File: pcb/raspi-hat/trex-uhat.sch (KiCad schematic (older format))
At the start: 17 parts, among them J1 Conn_01x08_Female, J10 RAIL2, J2 RPi_GPIO, J3 Conn_01x03_Female, J4 DFPLAYER_MINI, J5 RAIL1, J6 Conn_01x04_Female, J7 AudioJack3, J8 Jack-DC, J9 Conn_01x05_Female

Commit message: fix(pcb): motor connections, replace audio + power jacks
- Change power jack from PJ-063AH to the smaller PJ-102AH
- Change audio jack from SJ1-3533NG to PJ320E
- Fix motor connections: connect Pi to ~SLP instead of EN
- Improve DFPlayer Mini Footprint
- Add silk-screen texts
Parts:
- J7: footprint Connector_Audio:Jack_3.5mm_CUI_SJ1-3533NG_Horizontal -> Connector_Audio:Jack_3.5mm_PJ320E_Horizontal; symbol Connector:AudioJack3 -> Connector:AudioJack4
- J8: footprint Connector_BarrelJack:BarrelJack_CUI_PJ-063AH_Horizontal -> Connector_BarrelJack:BarrelJack_CUI_PJ-102AH_Horizontal
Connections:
- net labels added: STP1_~SLP, STP2_~SLP
- net labels removed: STP1_EN, STP2_EN
- wire segments 114 -> 118
- no-connect marks 36 -> 37
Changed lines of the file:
@@
 	7300 3300 6800 3300
 Text Label 6800 3300 0    50   ~ 0
-STP1_EN
+STP1_~SLP
 Wire Wire Line
 	7300 3400 6800 3400
@@
 STP1_STEP
 Wire Wire Line
-	3250 6050 2850 6050
-Wire Wire Line
-	3250 5850 2850 5850
-Text Label 2850 5850 0    50   ~ 0
-STP1_EN
-Text Label 2850 5950 0    50   ~ 0
+	3250 6050 2800 6050
+Text Label 2800 5650 0    50   ~ 0
+STP1_~SLP
+Text Label 2800 5950 0    50   ~ 0
 STP1_STEP
 Wire Wire Line
-	2850 5950 3250 5950
-Text Label 2850 6050 0    50   ~ 0
+	2800 5950 3250 5950
+Text Label 2800 6050 0    50   ~ 0
 STP1_DIR
-Wire Wire Line
-	4850 5900 5300 5900
-Text Label 4850 5900 0    50   ~ 0
-STP2_EN
+Text Label 4850 5700 0    50   ~ 0
+STP2_~SLP
 Wire Wire Line
 	5300 6000 4850 6000
@@
 	7300 4200 6800 4200
 Text Label 6800 4200 0    50   ~ 0
-STP2_EN
+STP2_~SLP
 Wire Wire Line
 	9200 4200 9650 4200
@@
 NoConn ~ 1650 2600
 $Comp
-L Connector:AudioJack3 J7
+L Connector:AudioJack4 J7
 U 1 1 5D77E4B7
 P 1100 3550
 F 0 "J7" V 1128 3320 50  0000 R CNN
 F 1 "AudioJack3" V 1037 3320 50  0000 R CNN
-F 2 "Connector_Audio:Jack_3.5mm_CUI_SJ1-3533NG_Horizontal" H 1100 3550 50  0001 C CNN
+F 2 "Connector_Audio:Jack_3.5mm_PJ320E_Horizontal" H 1100 3550 50  0001 C CNN
 F 3 "~" H 1100 3550 50  0001 C CNN
 	1    1100 3550
 	0    -1   -1   0
 $EndComp
-Wire Wire Line
-	1650 3100 1000 3100
-Wire Wire Line
-	1000 3100 1000 3350
-Wire Wire Line
-	1100 3350 1200 3350
-Wire Wire Line
-	1100 3350 1100 2900
-Wire Wire Line
-	1100 2900 1650 2900
-Connection ~ 1100 3350
 $Comp
 L Connector:Barrel_Jack_Switch J8
@@
 F 0 "J8" H 8970 1500 50  0000 R CNN
 F 1 "Jack-DC" H 8970 1591 50  0000 R CNN
-F 2 "Connector_BarrelJack:BarrelJack_CUI_PJ-063AH_Horizontal" H 9250 1510 50  0001 C CNN
+F 2 "Connector_BarrelJack:BarrelJack_CUI_PJ-102AH_Horizontal" H 9250 1510 50  0001 C CNN
 F 3 "~" H 9250 1510 50  0001 C CNN
 	1    9200 1550
@@
 NoConn ~ 3250 6450
 NoConn ~ 3250 6550
-NoConn ~ 3250 5650
+NoConn ~ 3250 5850
 NoConn ~ 3250 5550
 NoConn ~ 5300 5600
-NoConn ~ 5300 5700
+NoConn ~ 5300 5900
 $Comp
 L Connector:Conn_01x04_Female J10
@@
 	9450 4900 9300 4900
 $Comp
-L power:+3.3V #PWR?
+L power:+3.3V #PWR0106
 U 1 1 5D910A9E
 P 10150 5100
-F 0 "#PWR?" H 10150 4950 50  0001 C CNN
+F 0 "#PWR0106" H 10150 4950 50  0001 C CNN
 F 1 "+3.3V" H 10165 5273 50  0000 C CNN
 F 2 "" H 10150 5100 50  0001 C CNN
@@
 Wire Wire Line
 	10150 4900 10150 5100
+Wire Wire Line
+	1000 2900 1000 3250
+Wire Wire Line
+	1000 2900 1650 2900
+Wire Wire Line
+	1650 3100 1300 3100
+Wire Wire Line
+	1200 3100 1200 3350
+Wire Wire Line
+	1300 3350 1300 3100
+Connection ~ 1300 3100
+Wire Wire Line
+	1300 3100 1200 3100
+Wire Wire Line
+	1000 3250 1100 3250
+Wire Wire Line
+	1100 3250 1100 3350
+Connection ~ 1000 3250
+Wire Wire Line
+	1000 3250 1000 3350
+Wire Wire Line
+	3250 5650 2800 5650
+Wire Wire Line
+	5300 5700 4850 5700
+NoConn ~ 9750 5200
 $EndSCHEMATC

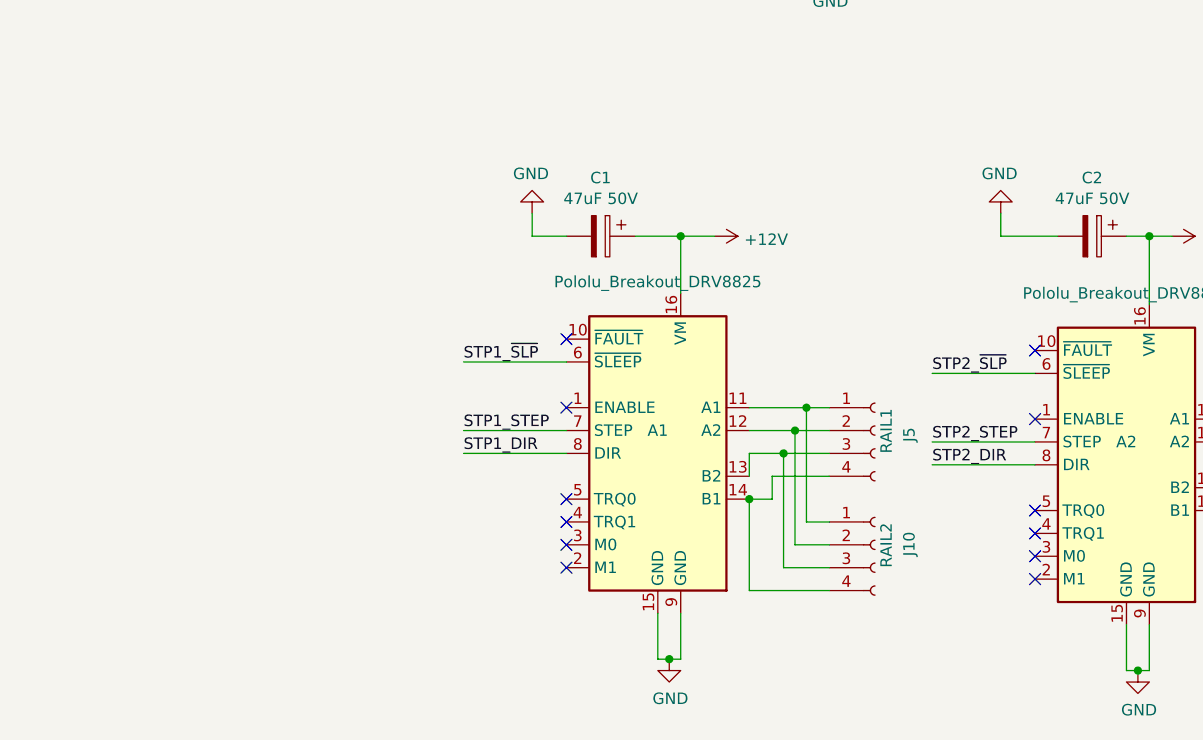
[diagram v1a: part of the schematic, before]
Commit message: feat(pcb): DRV8825 support
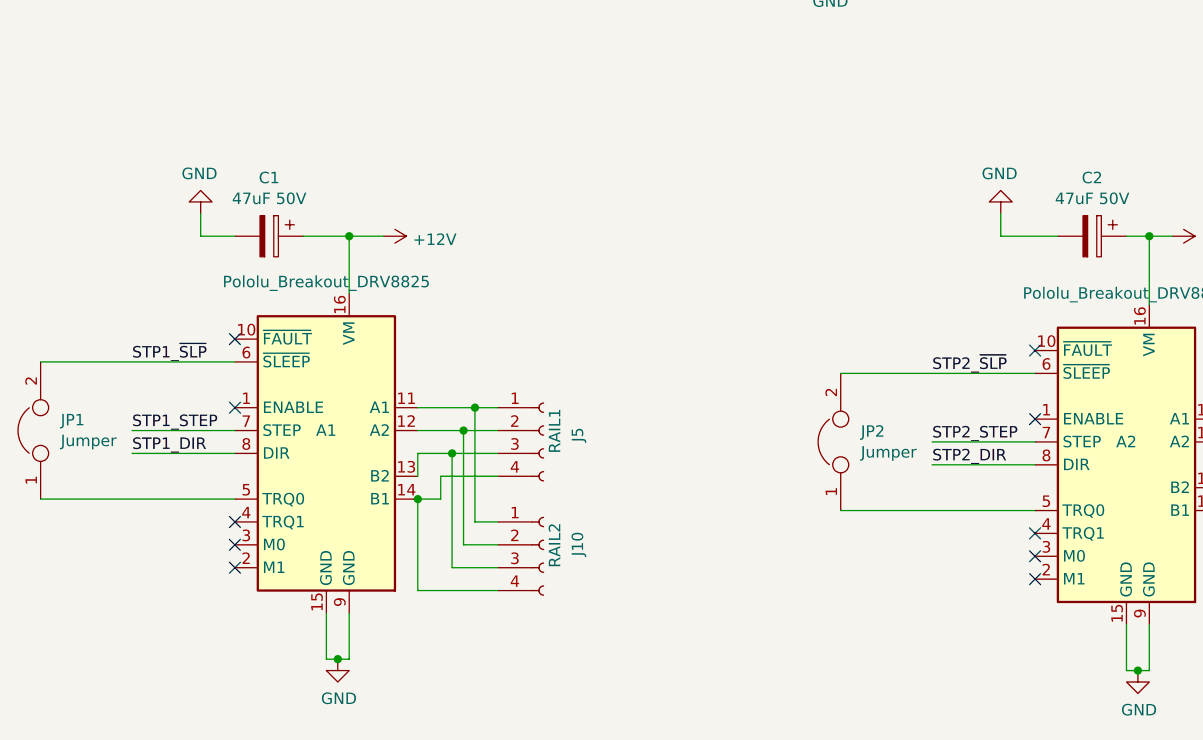
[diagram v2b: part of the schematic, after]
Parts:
- added JP1, JP2: Jumper, Jumper:SolderJumper-2_P1.3mm_Bridged_RoundedPad1.0x1.5mm, symbol Device:Jumper
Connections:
- wire segments 118 -> 120
- no-connect marks 37 -> 35
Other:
- moved on the sheet: A1, C1, J10, J5
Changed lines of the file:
@@
 L uhat:Pololu_Breakout_DRV8880 A1
 U 1 1 5D6AAAE1
-P 3650 5950
-F 0 "A1" H 3650 5950 50  0000 C CNN
-F 1 "Pololu_Breakout_DRV8825" H 3650 6600 50  0000 C CNN
-F 2 "Module:Pololu_Breakout-16_15.2x20.3mm" H 3850 5150 50  0001 L CNN
-F 3 "https://www.pololu.com/product/2982" H 3750 5650 50  0001 C CNN
-	1    3650 5950
+P 2200 5950
+F 0 "A1" H 2200 5950 50  0000 C CNN
+F 1 "Pololu_Breakout_DRV8825" H 2200 6600 50  0000 C CNN
+F 2 "Module:Pololu_Breakout-16_15.2x20.3mm" H 2400 5150 50  0001 L CNN
+F 3 "https://www.pololu.com/product/2982" H 2300 5650 50  0001 C CNN
+	1    2200 5950
 	1    0    0    -1
 $EndComp
@@
 L power:GND #PWR06
 U 1 1 5D6B2DDB
-P 3700 6950
-F 0 "#PWR06" H 3700 6700 50  0001 C CNN
-F 1 "GND" H 3705 6777 50  0000 C CNN
-F 2 "" H 3700 6950 50  0001 C CNN
-F 3 "" H 3700 6950 50  0001 C CNN
-	1    3700 6950
-	1    0    0    -1
-$EndComp
-Wire Wire Line
-	3750 6750 3750 6950
-Wire Wire Line
-	3750 6950 3700 6950
-Wire Wire Line
-	3700 6950 3650 6950
-Wire Wire Line
-	3650 6950 3650 6750
-Connection ~ 3700 6950
+P 2250 6950
+F 0 "#PWR06" H 2250 6700 50  0001 C CNN
+F 1 "GND" H 2255 6777 50  0000 C CNN
+F 2 "" H 2250 6950 50  0001 C CNN
+F 3 "" H 2250 6950 50  0001 C CNN
+	1    2250 6950
+	1    0    0    -1
+$EndComp
+Wire Wire Line
+	2300 6750 2300 6950
+Wire Wire Line
+	2300 6950 2250 6950
+Wire Wire Line
+	2250 6950 2200 6950
+Wire Wire Line
+	2200 6950 2200 6750
+Connection ~ 2250 6950
 $Comp
 L power:+12V #PWR011
@@
 L Device:CP C1
 U 1 1 5D6CC610
-P 3400 5100
-F 0 "C1" V 3145 5100 50  0000 C CNN
-F 1 "47uF 50V" V 3236 5100 50  0000 C CNN
-F 2 "Capacitor_THT:CP_Radial_D6.3mm_P2.50mm" H 3438 4950 50  0001 C CNN
-F 3 "~" H 3400 5100 50  0001 C CNN
-	1    3400 5100
+P 1950 5100
+F 0 "C1" V 1695 5100 50  0000 C CNN
+F 1 "47uF 50V" V 1786 5100 50  0000 C CNN
+F 2 "Capacitor_THT:CP_Radial_D6.3mm_P2.50mm" H 1988 4950 50  0001 C CNN
+F 3 "~" H 1950 5100 50  0001 C CNN
+	1    1950 5100
 	0    1    1    0
 $EndComp
@@
 L power:+12V #PWR08
 U 1 1 5D6CCA76
-P 3900 5100
-F 0 "#PWR08" H 3900 4950 50  0001 C CNN
-F 1 "+12V" V 3915 5228 50  0000 L CNN
-F 2 "" H 3900 5100 50  0001 C CNN
-F 3 "" H 3900 5100 50  0001 C CNN
-	1    3900 5100
-	0    1    1    0
-$EndComp
-Wire Wire Line
-	3900 5100 3750 5100
-Wire Wire Line
-	3750 5350 3750 5100
-Connection ~ 3750 5100
-Wire Wire Line
-	3750 5100 3550 5100
+P 2450 5100
+F 0 "#PWR08" H 2450 4950 50  0001 C CNN
+F 1 "+12V" V 2465 5228 50  0000 L CNN
+F 2 "" H 2450 5100 50  0001 C CNN
+F 3 "" H 2450 5100 50  0001 C CNN
+	1    2450 5100
+	0    1    1    0
+$EndComp
+Wire Wire Line
+	2450 5100 2300 5100
+Wire Wire Line
+	2300 5350 2300 5100
+Connection ~ 2300 5100
+Wire Wire Line
+	2300 5100 2100 5100
 Wire Wire Line
 	5700 5100 5800 5100
@@
 L power:GND #PWR05
 U 1 1 5D6D45D1
-P 3100 5000
-F 0 "#PWR05" H 3100 4750 50  0001 C CNN
-F 1 "GND" H 3105 4827 50  0000 C CNN
-F 2 "" H 3100 5000 50  0001 C CNN
-F 3 "" H 3100 5000 50  0001 C CNN
-	1    3100 5000
+P 1650 5000
+F 0 "#PWR05" H 1650 4750 50  0001 C CNN
+F 1 "GND" H 1655 4827 50  0000 C CNN
+F 2 "" H 1650 5000 50  0001 C CNN
+F 3 "" H 1650 5000 50  0001 C CNN
+	1    1650 5000
 	-1   0    0    1
 $EndComp
 Wire Wire Line
-	3250 5100 3100 5100
-Wire Wire Line
-	3100 5100 3100 5000
+	1800 5100 1650 5100
+Wire Wire Line
+	1650 5100 1650 5000
 $Comp
 L power:GND #PWR09
@@
 	6350 6300 6100 6300
 Wire Wire Line
-	4400 5950 4250 5950
-Wire Wire Line
-	4050 6050 4050 6150
-Wire Wire Line
-	4150 6250 4050 6250
+	2950 5950 2800 5950
+Wire Wire Line
+	2600 6050 2600 6150
+Wire Wire Line
+	2700 6250 2600 6250
 $Comp
 L power:+5V #PWR03
@@
 STP1_STEP
 Wire Wire Line
-	3250 6050 2800 6050
-Text Label 2800 5650 0    50   ~ 0
+	1800 6050 1350 6050
+Text Label 1350 5650 0    50   ~ 0
 STP1_~SLP
-Text Label 2800 5950 0    50   ~ 0
+Text Label 1350 5950 0    50   ~ 0
 STP1_STEP
 Wire Wire Line
-	2800 5950 3250 5950
-Text Label 2800 6050 0    50   ~ 0
+	1350 5950 1800 5950
+Text Label 1350 6050 0    50   ~ 0
 STP1_DIR
 Text Label 4850 5700 0    50   ~ 0
@@
 	8900 1550 8900 1450
 Connection ~ 8900 1450
-NoConn ~ 5300 6300
 NoConn ~ 5300 6400
 NoConn ~ 5300 6500
 NoConn ~ 5300 6600
-NoConn ~ 3250 6250
-NoConn ~ 3250 6350
-NoConn ~ 3250 6450
-NoConn ~ 3250 6550
-NoConn ~ 3250 5850
-NoConn ~ 3250 5550
+NoConn ~ 1800 6350
+NoConn ~ 1800 6450
+NoConn ~ 1800 6550
+NoConn ~ 1800 5850
+NoConn ~ 1800 5550
 NoConn ~ 5300 5600
 NoConn ~ 5300 5900
@@
 L Connector:Conn_01x04_Female J10
 U 1 1 5D85E9E8
-P 4600 6450
-F 0 "J10" V 4750 6400 50  0000 L CNN
-F 1 "RAIL2" V 4650 6350 50  0000 L CNN
-F 2 "Connector_PinSocket_2.54mm:PinSocket_1x04_P2.54mm_Vertical" H 4600 6450 50  0001 C CNN
-F 3 "~" H 4600 6450 50  0001 C CNN
-	1    4600 6450
-	1    0    0    -1
-$EndComp
-Wire Wire Line
-	4050 5850 4300 5850
+P 3150 6450
+F 0 "J10" V 3300 6400 50  0000 L CNN
+F 1 "RAIL2" V 3200 6350 50  0000 L CNN
+F 2 "Connector_PinSocket_2.54mm:PinSocket_1x04_P2.54mm_Vertical" H 3150 6450 50  0001 C CNN
+F 3 "~" H 3150 6450 50  0001 C CNN
+	1    3150 6450
+	1    0    0    -1
+$EndComp
+Wire Wire Line
+	2600 5850 2850 5850
 $Comp
 L Connector:Conn_01x04_Female J5
 U 1 1 5D6D6AFB
-P 4600 5950
-F 0 "J5" V 4750 5900 50  0000 L CNN
-F 1 "RAIL1" V 4650 5850 50  0000 L CNN
-F 2 "Connector_PinSocket_2.54mm:PinSocket_1x04_P2.54mm_Vertical" H 4600 5950 50  0001 C CNN
-F 3 "~" H 4600 5950 50  0001 C CNN
-	1    4600 5950
-	1    0    0    -1
-$EndComp
-Wire Wire Line
-	4400 6150 4150 6150
-Wire Wire Line
-	4050 6250 4050 6650
-Wire Wire Line
-	4050 6650 4400 6650
-Connection ~ 4050 6250
-Wire Wire Line
-	4400 6050 4200 6050
-Wire Wire Line
-	4150 6150 4150 6250
-Wire Wire Line
-	4400 6550 4200 6550
-Wire Wire Line
-	4200 6550 4200 6050
-Connection ~ 4200 6050
-Wire Wire Line
-	4200 6050 4050 6050
-Wire Wire Line
-	4400 6450 4250 6450
-Wire Wire Line
-	4250 6450 4250 5950
-Connection ~ 4250 5950
-Wire Wire Line
-	4250 5950 4050 5950
-Wire Wire Line
-	4300 5850 4300 6350
-Wire Wire Line
-	4300 6350 4400 6350
-Connection ~ 4300 5850
-Wire Wire Line
-	4300 5850 4400 5850
+P 3150 5950
+F 0 "J5" V 3300 5900 50  0000 L CNN
+F 1 "RAIL1" V 3200 5850 50  0000 L CNN
+F 2 "Connector_PinSocket_2.54mm:PinSocket_1x04_P2.54mm_Vertical" H 3150 5950 50  0001 C CNN
+F 3 "~" H 3150 5950 50  0001 C CNN
+	1    3150 5950
+	1    0    0    -1
+$EndComp
+Wire Wire Line
+	2950 6150 2700 6150
+Wire Wire Line
+	2600 6250 2600 6650
+Wire Wire Line
+	2600 6650 2950 6650
+Connection ~ 2600 6250
+Wire Wire Line
+	2950 6050 2750 6050
+Wire Wire Line
+	2700 6150 2700 6250
+Wire Wire Line
+	2950 6550 2750 6550
+Wire Wire Line
+	2750 6550 2750 6050
+Connection ~ 2750 6050
+Wire Wire Line
+	2750 6050 2600 6050
+Wire Wire Line
+	2950 6450 2800 6450
+Wire Wire Line
+	2800 6450 2800 5950
+Connection ~ 2800 5950
+Wire Wire Line
+	2800 5950 2600 5950
+Wire Wire Line
+	2850 5850 2850 6350
+Wire Wire Line
+	2850 6350 2950 6350
+Connection ~ 2850 5850
+Wire Wire Line
+	2850 5850 2950 5850
 Wire Wire Line
 	6950 1650 6950 1800
@@
 Wire Wire Line
 	1000 3250 1000 3350
-Wire Wire Line
-	3250 5650 2800 5650
-Wire Wire Line
-	5300 5700 4850 5700
 NoConn ~ 9750 5200
+$Comp
+L Device:Jumper JP1
+U 1 1 5D895BFF
+P 950 5950
+F 0 "JP1" V 996 5862 50  0000 R CNN
+F 1 "Jumper" V 905 5862 50  0000 R CNN
+F 2 "Jumper:SolderJumper-2_P1.3mm_Bridged_RoundedPad1.0x1.5mm" H 950 5950 50  0001 C CNN
+F 3 "~" H 950 5950 50  0001 C CNN
+	1    950  5950
+	0    -1   -1   0
+$EndComp
+Wire Wire Line
+	950  5650 1800 5650
+Wire Wire Line
+	950  6250 1800 6250
+$Comp
+L Device:Jumper JP2
+U 1 1 5D8AD796
+P 4450 6000
+F 0 "JP2" V 4496 5912 50  0000 R CNN
+F 1 "Jumper" V 4405 5912 50  0000 R CNN
+F 2 "Jumper:SolderJumper-2_P1.3mm_Bridged_RoundedPad1.0x1.5mm" H 4450 6000 50  0001 C CNN
+F 3 "~" H 4450 6000 50  0001 C CNN
+	1    4450 6000
+	0    -1   -1   0
+$EndComp
+Wire Wire Line
+	4450 5700 5300 5700
+Wire Wire Line
+	4450 6300 5300 6300
 $EndSCHEMATC
